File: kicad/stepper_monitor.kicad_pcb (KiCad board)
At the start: 2 copper layers, 1 part, among them U1 ESP32-WROOM-32

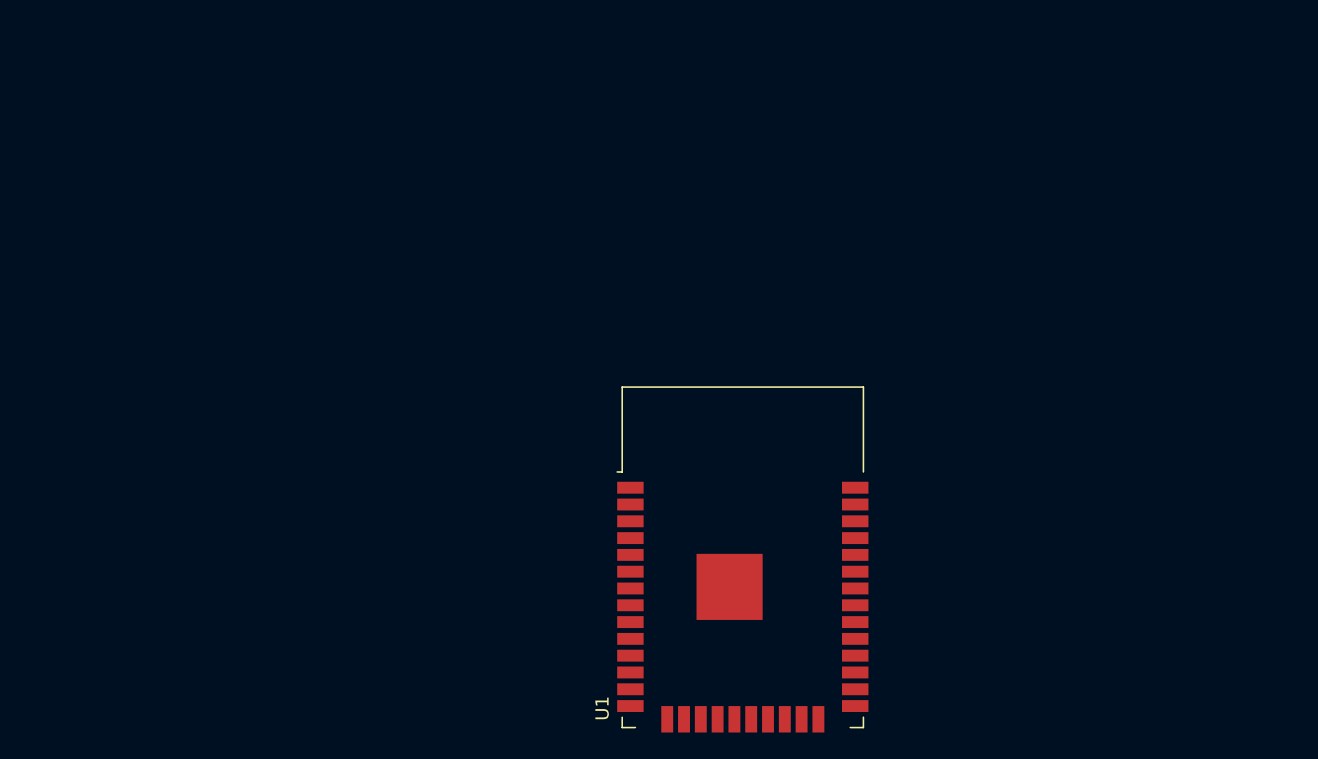
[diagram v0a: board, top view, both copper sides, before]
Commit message: Updated to Kicad 6
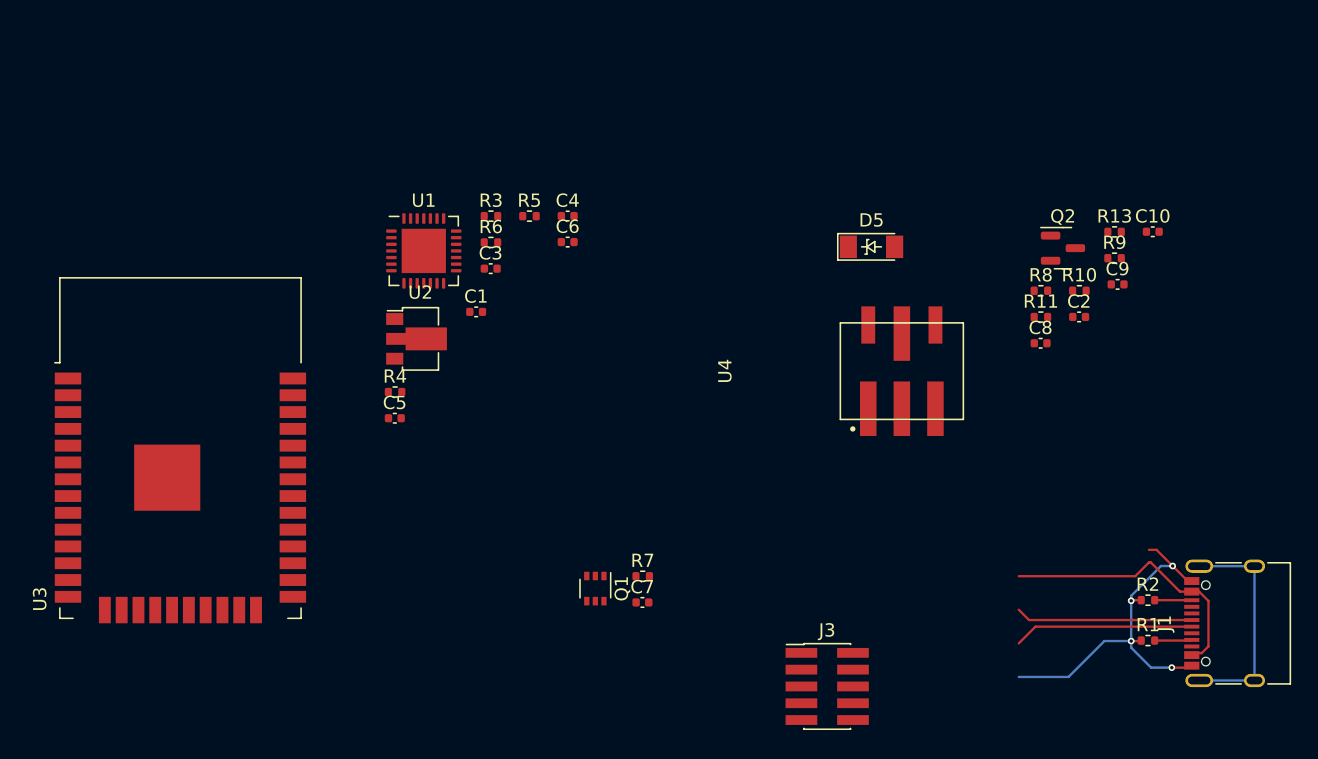
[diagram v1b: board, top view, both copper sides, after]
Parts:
- added C1: 100n, Capacitor_SMD:C_0402_1005Metric, F.Cu at (130.9, 79.6)
- added C10: 10u, Capacitor_SMD:C_0402_1005Metric, F.Cu at (182.1, 73.6)
- added C2: 10u 50V, Capacitor_SMD:C_0402_1005Metric, F.Cu at (176.5, 80.0)
- added C3: 10u, Capacitor_SMD:C_0402_1005Metric, F.Cu at (132.0, 76.4)
- added C4: 100n, Capacitor_SMD:C_0402_1005Metric, F.Cu at (137.9, 72.4)
- added C5: 100n, Capacitor_SMD:C_0402_1005Metric, F.Cu at (124.8, 87.7)
- added C6: 100n, Capacitor_SMD:C_0402_1005Metric, F.Cu at (137.9, 74.3)
- added C7: 10u, Capacitor_SMD:C_0402_1005Metric, F.Cu at (143.5, 101.6)
- added C8: 100n 50V, Capacitor_SMD:C_0402_1005Metric, F.Cu at (173.6, 82.0)
- added C9: 10u, Capacitor_SMD:C_0402_1005Metric, F.Cu at (179.4, 77.5)
- added D5: zenner, stepper_probe:D_MiniMELF_zenner, F.Cu at (160.8, 74.7)
- added J1: USB_C_Receptacle_USB2.0, stepper_monitor:USB_C_Receptacle_XKB_U262-16XN-4BVC11, F.Cu at (188.7, 103.2)
- added J3: Conn_02x05_Odd_Even, stepper_monitor:PinHeader_2x05_P1.27mm_Vertical_SMD, F.Cu at (157.5, 108.0)
- added Q1: UMH3N, Package_TO_SOT_SMD:SOT-363_SC-70-6, F.Cu at (139.9, 100.5)
- added Q2: P_MOSFET, Package_TO_SOT_SMD:SOT-23, F.Cu at (175.3, 74.8)
- added R1: 5K1, Resistor_SMD:R_0402_1005Metric, F.Cu at (181.7, 104.5)
- added R10: 10K, Resistor_SMD:R_0402_1005Metric, F.Cu at (176.6, 78.0)
- added R11: 10K, Resistor_SMD:R_0402_1005Metric, F.Cu at (173.6, 80.0)
- added R13: 20K, Resistor_SMD:R_0402_1005Metric, F.Cu at (179.2, 73.6)
- added R2: 5K1, Resistor_SMD:R_0402_1005Metric, F.Cu at (181.7, 101.4)
- added R3: 5K1, Resistor_SMD:R_0402_1005Metric, F.Cu at (132.1, 72.4)
- added R4: 5K1, Resistor_SMD:R_0402_1005Metric, F.Cu at (124.8, 85.7)
- added R5: 5K1, Resistor_SMD:R_0402_1005Metric, F.Cu at (135.0, 72.4)
- added R6: 5K1, Resistor_SMD:R_0402_1005Metric, F.Cu at (132.1, 74.4)
- added R7: 10K, Resistor_SMD:R_0402_1005Metric, F.Cu at (143.5, 99.6)
- added R8: 1K, Resistor_SMD:R_0402_1005Metric, F.Cu at (173.6, 78.0)
- added R9: 1K, Resistor_SMD:R_0402_1005Metric, F.Cu at (179.2, 75.6)
- added U2: HT75xx-1-SOT89, Package_TO_SOT_SMD:SOT-89-3, F.Cu at (126.4, 81.7)
- added U3: ESP32-WROOM-32D, RF_Module:ESP32-WROOM-32, F.Cu at (108.6, 92.9)
- added U4: DC_DC, stepper_probe:Converter_DCDC, F.Cu at (163.1, 84.1)
- U1: value ESP32-WROOM-32 -> CP2102N-A01-GQFN28; footprint RF_Module:ESP32-WROOM-32 -> Package_DFN_QFN:QFN-28-1EP_5x5mm_P0.5mm_EP3.35x3.35mm
- moved U1 35.6 mm to (127.0, 75.0)
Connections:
- U1 pad 1: Net-(U1-Pad1) -> unconnected-(U1-Pad1)
- U1 pad 10: Net-(U1-Pad10) -> unconnected-(U1-Pad10)
- U1 pad 11: Net-(U1-Pad11) -> unconnected-(U1-Pad11)
- U1 pad 12: Net-(U1-Pad12) -> unconnected-(U1-Pad12)
- U1 pad 13: Net-(U1-Pad13) -> unconnected-(U1-Pad13)
- U1 pad 14: Net-(U1-Pad14) -> unconnected-(U1-Pad14)
- U1 pad 15: Net-(U1-Pad1) -> unconnected-(U1-Pad15)
- U1 pad 16: Net-(U1-Pad16) -> unconnected-(U1-Pad16)
- U1 pad 17: Net-(U1-Pad17) -> unconnected-(U1-Pad17)
- U1 pad 18: Net-(U1-Pad18) -> unconnected-(U1-Pad18)
- U1 pad 19: Net-(U1-Pad19) -> unconnected-(U1-Pad19)
- U1 pad 2: Net-(U1-Pad2) -> unconnected-(U1-Pad2)
- U1 pad 20: Net-(U1-Pad20) -> unconnected-(U1-Pad20)
- U1 pad 21: Net-(U1-Pad21) -> unconnected-(U1-Pad21)
- U1 pad 22: Net-(U1-Pad22) -> unconnected-(U1-Pad22)
- U1 pad 23: Net-(U1-Pad23) -> unconnected-(U1-Pad23)
- U1 pad 24: Net-(U1-Pad24) -> /RTS
- U1 pad 27: Net-(U1-Pad27) -> unconnected-(U1-Pad27)
- U1 pad 28: Net-(U1-Pad28) -> /DTR
- U1 pad 29: Net-(U1-Pad29) -> GNDD
- U1 pad 3: Net-(U1-Pad3) -> GNDD
- U1 pad 4: Net-(U1-Pad4) -> /D+
- U1 pad 5: Net-(U1-Pad5) -> /D-
- U1 pad 6: Net-(U1-Pad6) -> +3V3
- U1 pad 7: Net-(U1-Pad7) -> +3V3
- U1 pad 8: Net-(U1-Pad8) -> /VBUS
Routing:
- net GNDD: track 0.00 -> 29.1 mm, vias 0 -> 4
- net /VBUS: track 0.00 -> 21.2 mm
- net unconnected-(J1-PadS1): track 0.00 -> 17.0 mm
- net /D+: track 0.00 -> 13.6 mm
- net /D-: track 0.00 -> 13.4 mm
- net Net-(J1-PadA5): track 0.00 -> 2.82 mm
- net Net-(J1-PadB5): track 0.00 -> 2.80 mm
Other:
- net class Default removed

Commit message: Work in progress.
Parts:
- added C11: 100n, Capacitor_SMD:C_0402_1005Metric, F.Cu at (130.8, 62.2)
- added C12: DNP, Capacitor_SMD:C_0402_1005Metric, F.Cu at (116.8, 68.7)
- added C13: 100n, Capacitor_SMD:C_0402_1005Metric, F.Cu at (119.7, 66.7)
- added C14: DNP, Capacitor_SMD:C_0402_1005Metric, F.Cu at (122.6, 66.7)
- added R14: 1K, Resistor_SMD:R_0402_1005Metric, F.Cu at (130.8, 60.2)
- added R15: 1K, Resistor_SMD:R_0402_1005Metric, F.Cu at (116.8, 66.7)
- added R16: DNP, Resistor_SMD:R_0402_1005Metric, F.Cu at (113.9, 68.7)
- added R17: DNP, Resistor_SMD:R_0402_1005Metric, F.Cu at (113.9, 66.7)
- added U5: CC6920BSO-5A, Package_SO:SOIC-8_3.9x4.9mm_P1.27mm, F.Cu at (116.7, 62.5)
- added U6: CC6920BSO-5A, Package_SO:SOIC-8_3.9x4.9mm_P1.27mm, F.Cu at (125.2, 62.5)
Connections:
- C3 pad 2: +3V3 -> Net-(C3-Pad2)
- C4 pad 2: +3V3 -> Net-(C3-Pad2)
- J3 pad 1: unconnected-(J3-Pad1) -> +3V3
- J3 pad 2: unconnected-(J3-Pad2) -> /ESP_TMS
- J3 pad 3: unconnected-(J3-Pad3) -> GNDD
- J3 pad 4: unconnected-(J3-Pad4) -> /ESP_TCK
- J3 pad 5: unconnected-(J3-Pad5) -> GNDD
- J3 pad 6: unconnected-(J3-Pad6) -> /ESP_TDO
- J3 pad 7: unconnected-(J3-Pad7) -> GNDD
- J3 pad 8: unconnected-(J3-Pad8) -> /ESP_TDI
- J3 pad 9: unconnected-(J3-Pad9) -> GNDD
- U2 pad 3: +3V3 -> Net-(C3-Pad2)
- U3 pad 13: unconnected-(U3-Pad13) -> /ESP_TMS
- U3 pad 14: unconnected-(U3-Pad14) -> /ESP_TDI
- U3 pad 16: unconnected-(U3-Pad16) -> /ESP_TCK
- U3 pad 23: unconnected-(U3-Pad23) -> /ESP_TDO
